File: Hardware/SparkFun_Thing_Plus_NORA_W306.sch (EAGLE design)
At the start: 75 parts, among them J1 THING_PLUS_LOGICAL, J2 LiPo, J3 QWIIC_RA, J4 MICRO-SDFRICTION, J5 USB-C, Q1 3.1A/30V/105mΩ, Q2 MBT3904DW1T1, U1 UBLOX_NORA_W306, U3 XC6222B331MR-G, U4 MCP73831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

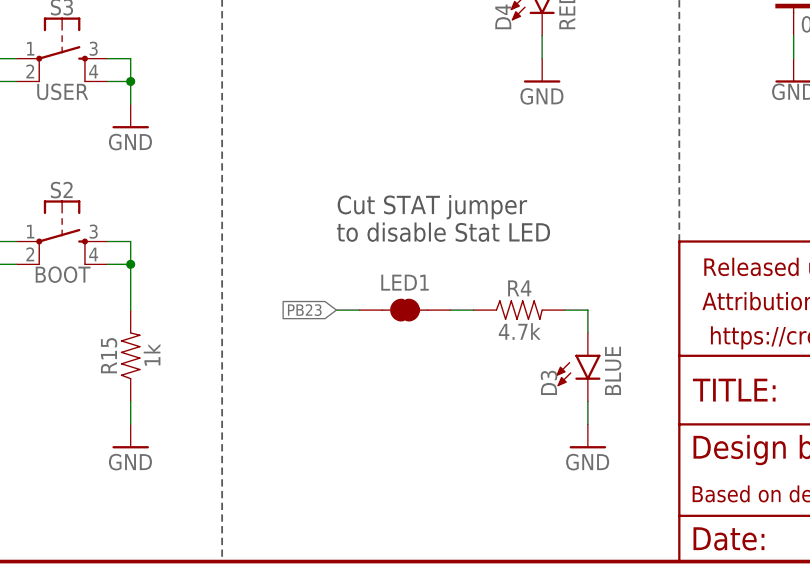
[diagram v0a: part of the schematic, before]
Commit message: Renamed and updated label to STAT Jumper to JP4
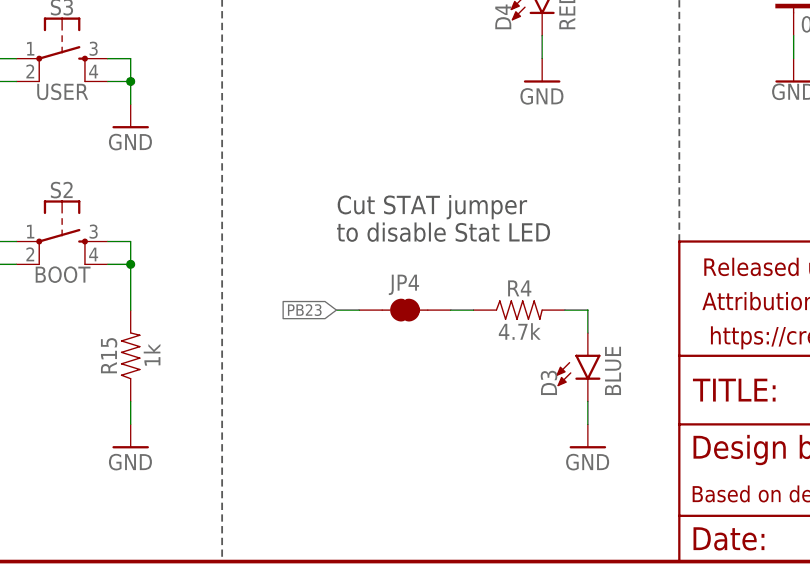
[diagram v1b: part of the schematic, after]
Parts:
- renumbered LED1 to JP4

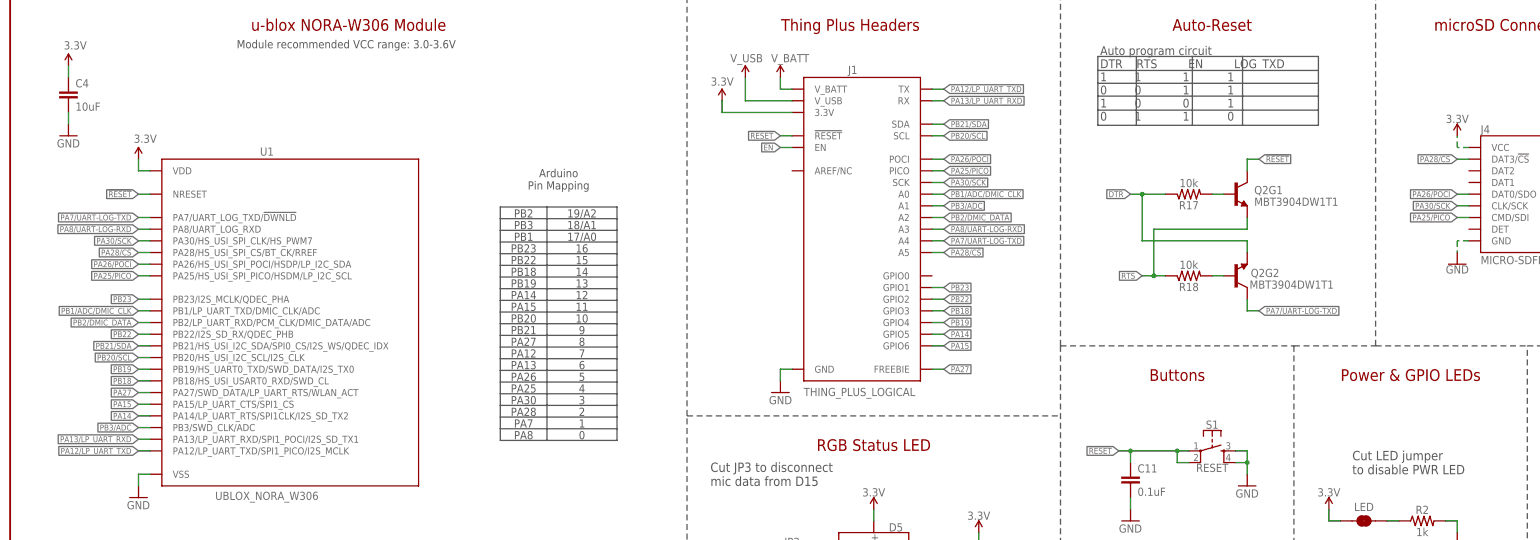
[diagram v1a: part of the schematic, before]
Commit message: Switched to SPI1 and alternate TX1/RX1 pins
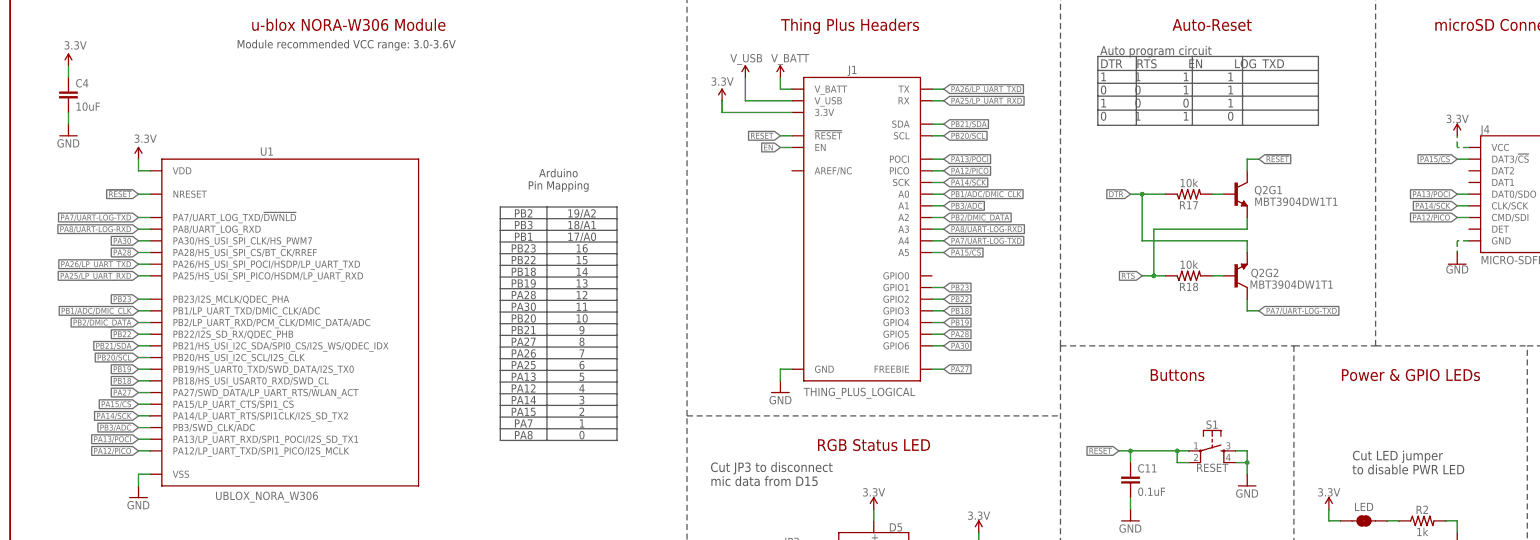
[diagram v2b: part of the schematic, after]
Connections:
- removed net PA12/LP_UART_TXD: J1.TX, U1.PA12/LP_UART_TXD/SPI1_PICO/I2S_MCLK
- removed net PA13/LP_UART_RXD: J1.RX, U1.PA13/LP_UART_RXD/SPI1_POCI/I2S_SD_TX1
- removed net PA14: J1.GPIO5, U1.PA14/LP_UART_RTS/SPI1CLK/I2S_SD_TX2
- removed net PA15: J1.GPIO6, U1.PA15/LP_UART_CTS/SPI1_CS
- removed net PA25/PICO: J1.PICO, J4.CMD/SDI, U1.PA25/HS_USI_SPI_PICO/HSDM/LP_I2C_SCL
- removed net PA26/POCI: J1.POCI, J4.DAT0/SDO, U1.PA26/HS_USI_SPI_POCI/HSDP/LP_I2C_SDA
- removed net PA28/CS: J1.A5, J4.DAT3/!CS!, U1.PA28/HS_USI_SPI_CS/BT_CK/RREF
- removed net PA30/SCK: J1.SCK, J4.CLK/SCK, U1.PA30/HS_USI_SPI_CLK/HS_PWM7
- new net PA12/PICO: J1.PICO, J4.CMD/SDI, U1.PA12/LP_UART_TXD/SPI1_PICO/I2S_MCLK
- new net PA13/POCI: J1.POCI, J4.DAT0/SDO, U1.PA13/LP_UART_RXD/SPI1_POCI/I2S_SD_TX1
- new net PA14/SCK: J1.SCK, J4.CLK/SCK, U1.PA14/LP_UART_RTS/SPI1CLK/I2S_SD_TX2
- new net PA15/CS: J1.A5, J4.DAT3/!CS!, U1.PA15/LP_UART_CTS/SPI1_CS
- new net PA25/LP_UART_RXD: J1.RX, U1.PA25/HS_USI_SPI_PICO/HSDM/LP_UART_RXD
- new net PA26/LP_UART_TXD: J1.TX, U1.PA26/HS_USI_SPI_POCI/HSDP/LP_UART_TXD
- new net PA28: J1.GPIO5, U1.PA28/HS_USI_SPI_CS/BT_CK/RREF
- new net PA30: J1.GPIO6, U1.PA30/HS_USI_SPI_CLK/HS_PWM7
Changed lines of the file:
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@@
 <text x="111.76" y="86.36" size="1.778" layer="97" font="vector" align="bottom-center">PA8</text>
 <text x="111.76" y="88.9" size="1.778" layer="97" font="vector" align="bottom-center">PA7</text>
-<text x="111.76" y="91.44" size="1.778" layer="97" font="vector" align="bottom-center">PA28</text>
-<text x="111.76" y="93.98" size="1.778" layer="97" font="vector" align="bottom-center">PA30</text>
-<text x="111.76" y="96.52" size="1.778" layer="97" font="vector" align="bottom-center">PA25</text>
-<text x="111.76" y="99.06" size="1.778" layer="97" font="vector" align="bottom-center">PA26</text>
-<text x="111.76" y="101.6" size="1.778" layer="97" font="vector" align="bottom-center">PA13</text>
-<text x="111.76" y="104.14" size="1.778" layer="97" font="vector" align="bottom-center">PA12</text>
+<text x="111.76" y="91.44" size="1.778" layer="97" font="vector" align="bottom-center">PA15</text>
+<text x="111.76" y="93.98" size="1.778" layer="97" font="vector" align="bottom-center">PA14</text>
+<text x="111.76" y="96.52" size="1.778" layer="97" font="vector" align="bottom-center">PA12</text>
+<text x="111.76" y="99.06" size="1.778" layer="97" font="vector" align="bottom-center">PA13</text>
+<text x="111.76" y="101.6" size="1.778" layer="97" font="vector" align="bottom-center">PA25</text>
+<text x="111.76" y="104.14" size="1.778" layer="97" font="vector" align="bottom-center">PA26</text>
 <text x="111.76" y="106.68" size="1.778" layer="97" font="vector" align="bottom-center">PA27</text>
 <text x="111.76" y="109.22" size="1.778" layer="97" font="vector" align="bottom-center">PB21</text>
 <text x="111.76" y="111.76" size="1.778" layer="97" font="vector" align="bottom-center">PB20</text>
-<text x="111.76" y="114.3" size="1.778" layer="97" font="vector" align="bottom-center">PA15</text>
-<text x="111.76" y="116.84" size="1.778" layer="97" font="vector" align="bottom-center">PA14</text>
+<text x="111.76" y="114.3" size="1.778" layer="97" font="vector" align="bottom-center">PA30</text>
+<text x="111.76" y="116.84" size="1.778" layer="97" font="vector" align="bottom-center">PA28</text>
 <text x="111.76" y="119.38" size="1.778" layer="97" font="vector" align="bottom-center">PB19</text>
 <text x="111.76" y="121.92" size="1.778" layer="97" font="vector" align="bottom-center">PB18</text>
@@
 </segment>
 </net>
-<net name="PA30/SCK" class="0">
-<segment>
-<pinref part="U1" gate="G$1" pin="PA30/HS_USI_SPI_CLK/HS_PWM7"/>
-<wire x1="30.48" y1="129.54" x2="27.94" y2="129.54" width="0.1524" layer="91"/>
-<label x="27.94" y="129.54" size="1.27" layer="95" font="vector" rot="R180" xref="yes"/>
-</segment>
+<net name="PA14/SCK" class="0">
 <segment>
 <wire x1="200.66" y1="142.24" x2="203.2" y2="142.24" width="0.1524" layer="91"/>
@@
 <pinref part="J4" gate="J1" pin="CLK/SCK"/>
 </segment>
-</net>
-<net name="PA28/CS" class="0">
-<segment>
-<pinref part="U1" gate="G$1" pin="PA28/HS_USI_SPI_CS/BT_CK/RREF"/>
-<wire x1="30.48" y1="127" x2="27.94" y2="127" width="0.1524" layer="91"/>
-<label x="27.94" y="127" size="1.27" layer="95" font="vector" rot="R180" xref="yes"/>
-</segment>
+<segment>
+<pinref part="U1" gate="G$1" pin="PA14/LP_UART_RTS/SPI1CLK/I2S_SD_TX2"/>
+<wire x1="30.48" y1="91.44" x2="27.94" y2="91.44" width="0.1524" layer="91"/>
+<label x="27.94" y="91.44" size="1.27" layer="95" font="vector" rot="R180" xref="yes"/>
+</segment>
+</net>
+<net name="PA15/CS" class="0">
 <segment>
 <label x="203.2" y="127" size="1.27" layer="95" font="vector" rot="MR180" xref="yes"/>
@@
 <wire x1="317.5" y1="147.32" x2="314.96" y2="147.32" width="0.1524" layer="91"/>
 </segment>
-</net>
-<net name="PA26/POCI" class="0">
-<segment>
-<pinref part="U1" gate="G$1" pin="PA26/HS_USI_SPI_POCI/HSDP/LP_I2C_SDA"/>
-<wire x1="30.48" y1="124.46" x2="27.94" y2="124.46" width="0.1524" layer="91"/>
-<label x="27.94" y="124.46" size="1.27" layer="95" font="vector" rot="R180" xref="yes"/>
-</segment>
+<segment>
+<pinref part="U1" gate="G$1" pin="PA15/LP_UART_CTS/SPI1_CS"/>
+<wire x1="30.48" y1="93.98" x2="27.94" y2="93.98" width="0.1524" layer="91"/>
+<label x="27.94" y="93.98" size="1.27" layer="95" font="vector" rot="R180" xref="yes"/>
+</segment>
+</net>
+<net name="PA13/POCI" class="0">
 <segment>
 <wire x1="200.66" y1="147.32" x2="203.2" y2="147.32" width="0.1524" layer="91"/>
@@
 <pinref part="J4" gate="J1" pin="DAT0/SDO"/>
 </segment>
-</net>
-<net name="PA25/PICO" class="0">
-<segment>
-<pinref part="U1" gate="G$1" pin="PA25/HS_USI_SPI_PICO/HSDM/LP_I2C_SCL"/>
-<wire x1="30.48" y1="121.92" x2="27.94" y2="121.92" width="0.1524" layer="91"/>
-<label x="27.94" y="121.92" size="1.27" layer="95" font="vector" rot="R180" xref="yes"/>
-</segment>
+<segment>
+<pinref part="U1" gate="G$1" pin="PA13/LP_UART_RXD/SPI1_POCI/I2S_SD_TX1"/>
+<wire x1="30.48" y1="86.36" x2="27.94" y2="86.36" width="0.1524" layer="91"/>
+<label x="27.94" y="86.36" size="1.27" layer="95" font="vector" rot="R180" xref="yes"/>
+</segment>
+</net>
+<net name="PA12/PICO" class="0">
 <segment>
 <wire x1="200.66" y1="144.78" x2="203.2" y2="144.78" width="0.1524" layer="91"/>
@@
 <pinref part="J4" gate="J1" pin="CMD/SDI"/>
 </segment>
-</net>
-<net name="PA13/LP_UART_RXD" class="0">
-<segment>
-<pinref part="U1" gate="G$1" pin="PA13/LP_UART_RXD/SPI1_POCI/I2S_SD_TX1"/>
-<wire x1="30.48" y1="86.36" x2="27.94" y2="86.36" width="0.1524" layer="91"/>
-<label x="27.94" y="86.36" size="1.27" layer="95" font="vector" rot="R180" xref="yes"/>
-</segment>
-<segment>
-<wire x1="200.66" y1="160.02" x2="203.2" y2="160.02" width="0.1524" layer="91"/>
-<label x="203.2" y="160.02" size="1.27" layer="95" font="vector" xref="yes"/>
-<pinref part="J1" gate="G$1" pin="RX"/>
-</segment>
-</net>
-<net name="PA12/LP_UART_TXD" class="0">
 <segment>
 <pinref part="U1" gate="G$1" pin="PA12/LP_UART_TXD/SPI1_PICO/I2S_MCLK"/>
@@
 <label x="27.94" y="83.82" size="1.27" layer="95" font="vector" rot="R180" xref="yes"/>
 </segment>
+</net>
+<net name="PA26/LP_UART_TXD" class="0">
 <segment>
 <wire x1="200.66" y1="162.56" x2="203.2" y2="162.56" width="0.1524" layer="91"/>
@@
 <pinref part="J1" gate="G$1" pin="TX"/>
 </segment>
-</net>
-<net name="PA14" class="0">
-<segment>
-<pinref part="U1" gate="G$1" pin="PA14/LP_UART_RTS/SPI1CLK/I2S_SD_TX2"/>
-<wire x1="30.48" y1="91.44" x2="27.94" y2="91.44" width="0.1524" layer="91"/>
-<label x="27.94" y="91.44" size="1.27" layer="95" font="vector" rot="R180" xref="yes"/>
-</segment>
-<segment>
-<pinref part="J1" gate="G$1" pin="GPIO5"/>
-<wire x1="200.66" y1="109.22" x2="203.2" y2="109.22" width="0.1524" layer="91"/>
-<label x="203.2" y="109.22" size="1.27" layer="95" font="vector" xref="yes"/>
-</segment>
-</net>
-<net name="PA15" class="0">
-<segment>
-<pinref part="U1" gate="G$1" pin="PA15/LP_UART_CTS/SPI1_CS"/>
-<wire x1="30.48" y1="93.98" x2="27.94" y2="93.98" width="0.1524" layer="91"/>
-<label x="27.94" y="93.98" size="1.27" layer="95" font="vector" rot="R180" xref="yes"/>
-</segment>
-<segment>
-<pinref part="J1" gate="G$1" pin="GPIO6"/>
-<wire x1="200.66" y1="106.68" x2="203.2" y2="106.68" width="0.1524" layer="91"/>
-<label x="203.2" y="106.68" size="1.27" layer="95" font="vector" xref="yes"/>
+<segment>
+<pinref part="U1" gate="G$1" pin="PA26/HS_USI_SPI_POCI/HSDP/LP_UART_TXD"/>
+<wire x1="30.48" y1="124.46" x2="27.94" y2="124.46" width="0.1524" layer="91"/>
+<label x="27.94" y="124.46" size="1.27" layer="95" font="vector" rot="R180" xref="yes"/>
 </segment>
 </net>
@@
 </segment>
 </net>
+<net name="PA30" class="0">
+<segment>
+<pinref part="U1" gate="G$1" pin="PA30/HS_USI_SPI_CLK/HS_PWM7"/>
+<wire x1="30.48" y1="129.54" x2="27.94" y2="129.54" width="0.1524" layer="91"/>
+<label x="27.94" y="129.54" size="1.27" layer="95" font="vector" rot="R180" xref="yes"/>
+</segment>
+<segment>
+<wire x1="200.66" y1="106.68" x2="203.2" y2="106.68" width="0.1524" layer="91"/>
+<label x="203.2" y="106.68" size="1.27" layer="95" font="vector" xref="yes"/>
+<pinref part="J1" gate="G$1" pin="GPIO6"/>
+</segment>
+</net>
+<net name="PA28" class="0">
+<segment>
+<pinref part="U1" gate="G$1" pin="PA28/HS_USI_SPI_CS/BT_CK/RREF"/>
+<wire x1="30.48" y1="127" x2="27.94" y2="127" width="0.1524" layer="91"/>
+<label x="27.94" y="127" size="1.27" layer="95" font="vector" rot="R180" xref="yes"/>
+</segment>
+<segment>
+<wire x1="200.66" y1="109.22" x2="203.2" y2="109.22" width="0.1524" layer="91"/>
+<label x="203.2" y="109.22" size="1.27" layer="95" font="vector" xref="yes"/>
+<pinref part="J1" gate="G$1" pin="GPIO5"/>
+</segment>
+</net>
+<net name="PA25/LP_UART_RXD" class="0">
+<segment>
+<pinref part="U1" gate="G$1" pin="PA25/HS_USI_SPI_PICO/HSDM/LP_UART_RXD"/>
+<wire x1="30.48" y1="121.92" x2="27.94" y2="121.92" width="0.1524" layer="91"/>
+<label x="27.94" y="121.92" size="1.27" layer="95" font="vector" rot="R180" xref="yes"/>
+</segment>
+<segment>
+<wire x1="200.66" y1="160.02" x2="203.2" y2="160.02" width="0.1524" layer="91"/>
+<label x="203.2" y="160.02" size="1.27" layer="95" font="vector" xref="yes"/>
+<pinref part="J1" gate="G$1" pin="RX"/>
+</segment>
+</net>

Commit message: bumping version to v02
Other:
- note added: "v02"
- note removed: "v01"
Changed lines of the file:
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@@
 <text x="73.66" y="175.26" size="2.54" layer="94" font="vector" align="bottom-center">u-blox NORA-W306 Module</text>
 <text x="182.88" y="175.26" size="2.54" layer="94" font="vector" align="bottom-center">Thing Plus Headers</text>
-<text x="421.894" y="9.398" size="2.54" layer="94" font="vector" align="top-left">v01</text>
+<text x="421.894" y="9.398" size="2.54" layer="94" font="vector" align="top-left">v02</text>
 <text x="391.16" y="175.26" size="2.54" layer="94" font="vector" align="bottom-center">QWIIC Connector &amp; I2C Pullups</text>
 <text x="353.314" y="11.43" size="2.54" layer="94" font="vector">Pete Lewis</text>

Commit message: BOM consolidation
-added surface finish instructions (HASL)
-removed layer 100
-all 0.1uF caps are now the same 16V part (there used to be 3 different types).
-all 10uF are now the same part (just changed one cap from 0603 to 0402, but had the same voltage rating).
-all 4.7uF are now 0603, 35V, to accommodate VBATT inputs.
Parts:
- C11: device SparkFun-Capacitors:0.1UF-0402T-10V-10%-X7R -> SparkFun-Capacitors:0.1UF-0402T-16V-10%
- C19, C3, C6: device SparkFun-Capacitors:4.7UF-0402_TIGHT-6.3V-20%-X5R -> SparkFun-Capacitors:4.7UF-0603-35V-(20%)
- C4: device SparkFun-Capacitors:10UF-0603-6.3V-20% -> SparkFun-Capacitors:10UF-0402T-6.3V-20%
- C8: device SparkFun-Capacitors:0.1UF-0402T-6.3V-10%-X7R -> SparkFun-Capacitors:0.1UF-0402T-16V-10%

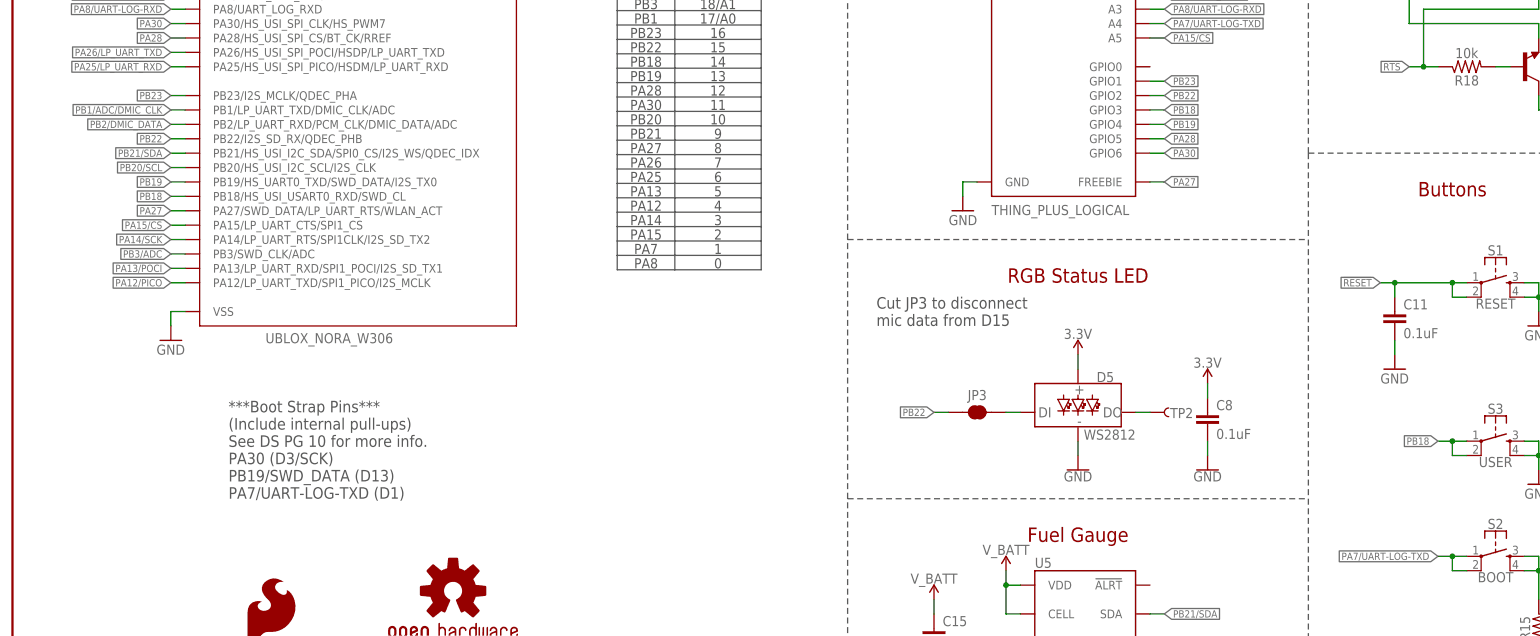
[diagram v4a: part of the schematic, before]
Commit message: Added SWD header to bottom side
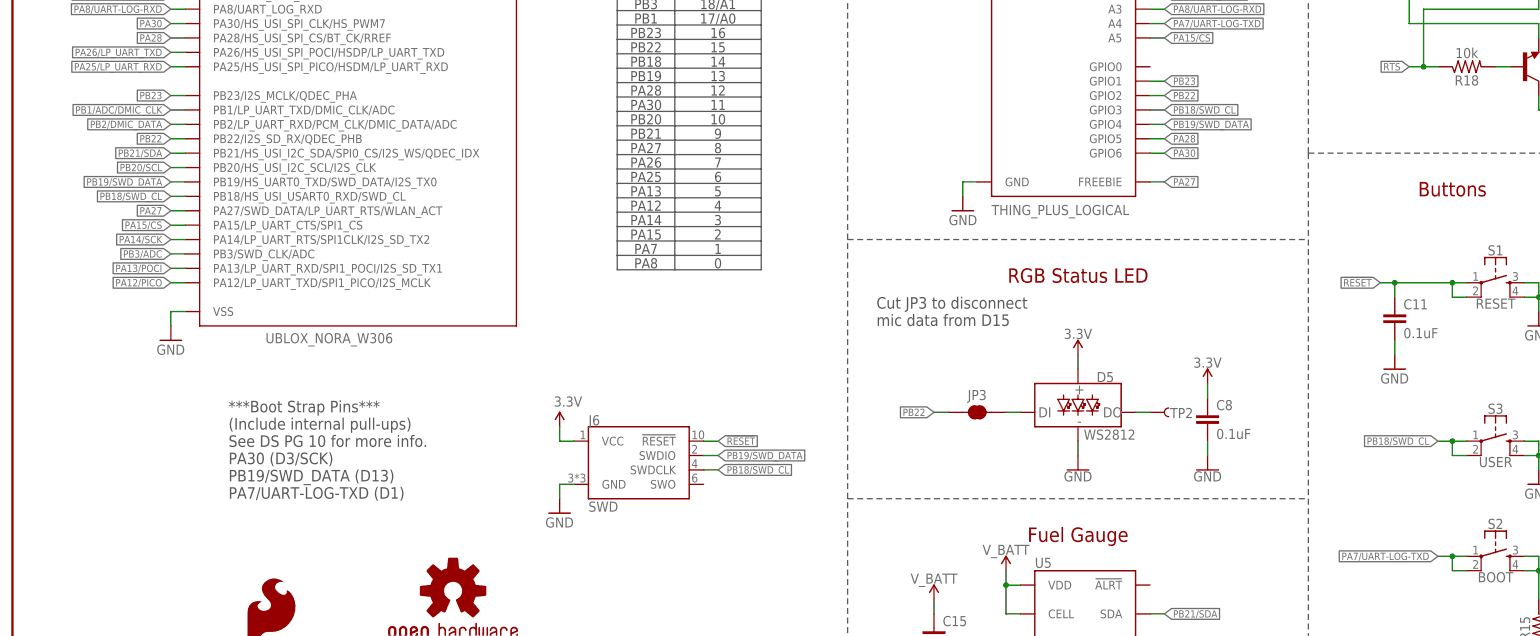
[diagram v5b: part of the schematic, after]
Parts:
- added J6: SWD, SparkFun-Connectors:CORTEX_JTAG_DEBUG_MINIMUM_SMD-UNSHROUDED
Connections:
- removed net PB18: J1.GPIO3, S3.1, S3.2, U1.PB18/HS_USI_USART0_RXD/SWD_CL
- removed net PB19: J1.GPIO4, U1.PB19/HS_UART0_TXD/SWD_DATA/I2S_TX0
- new net PB18/SWD_CL: J1.GPIO3, J6.SWDCLK, S3.1, S3.2, U1.PB18/HS_USI_USART0_RXD/SWD_CL
- new net PB19/SWD_DATA: J1.GPIO4, J6.SWDIO, U1.PB19/HS_UART0_TXD/SWD_DATA/I2S_TX0
- net !RESET!: now also J6.!RESET
- net 3.3V: now also J6.VCC
- net GND: now also J6.GND
